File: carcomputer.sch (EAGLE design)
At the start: 76 parts, among them IC1 LM358N, K1 351, K2 RT184012, K3 RT184012, Q1 BS170, Q5 TIP136, T1 BC618, T2 BC618, T3 BC618, T4 BC618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

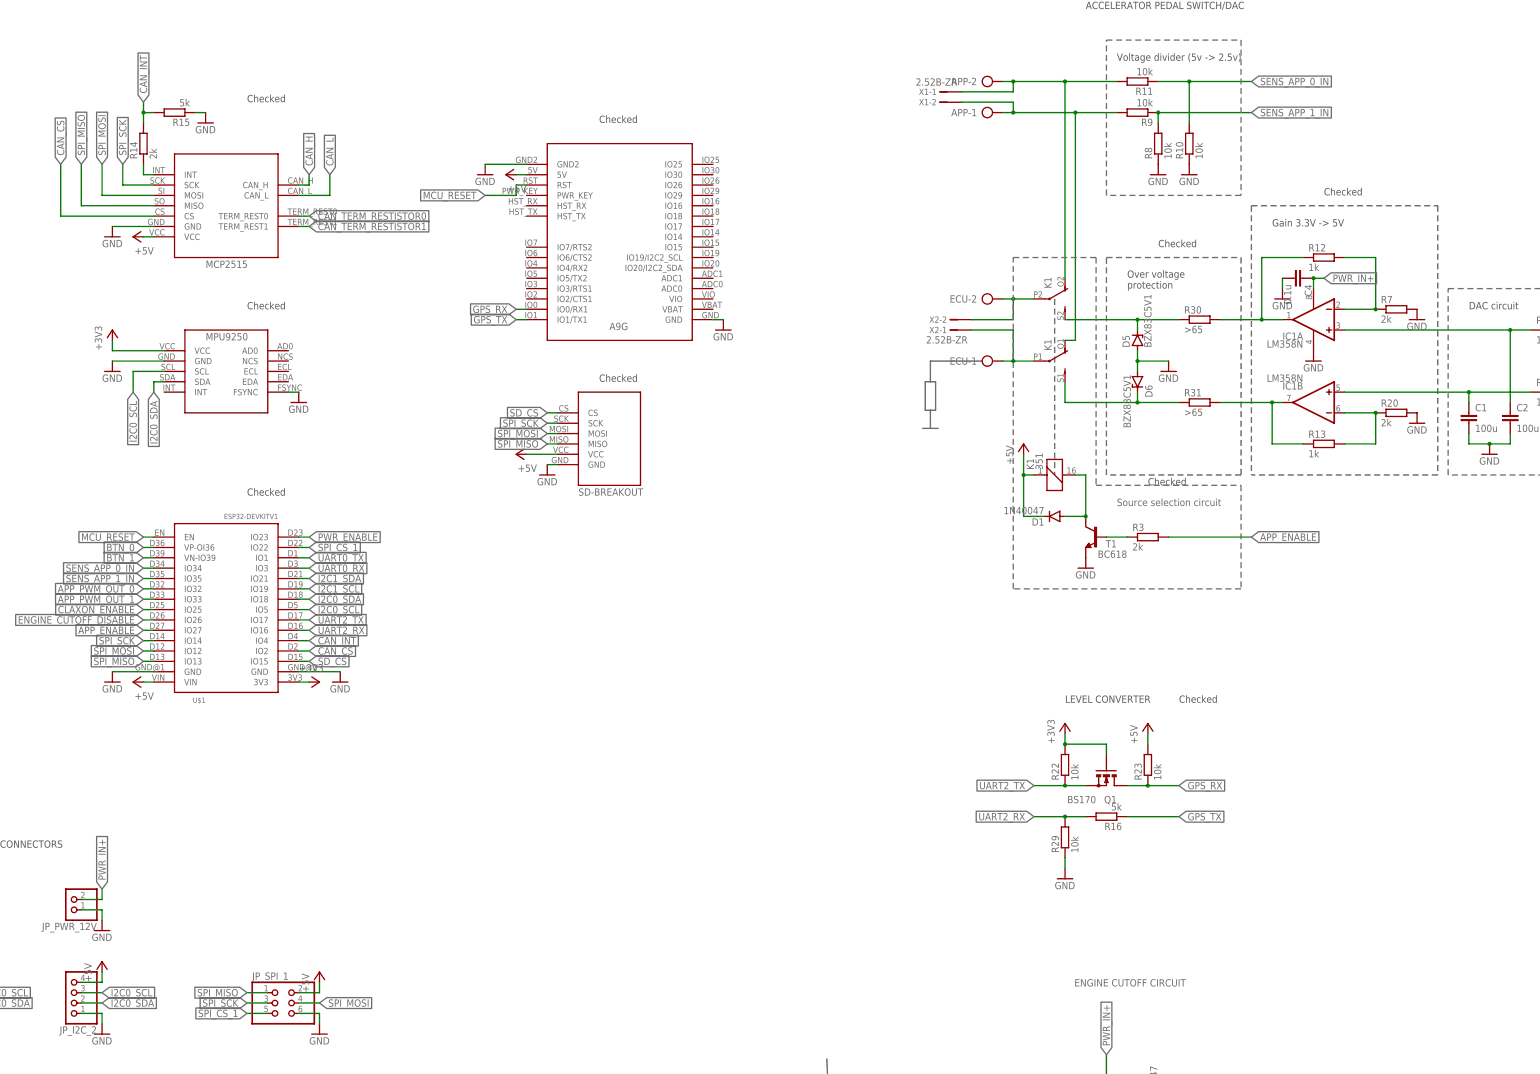
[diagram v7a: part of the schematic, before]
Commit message: Added volage divider for MISO. Also added more space to some tracks.
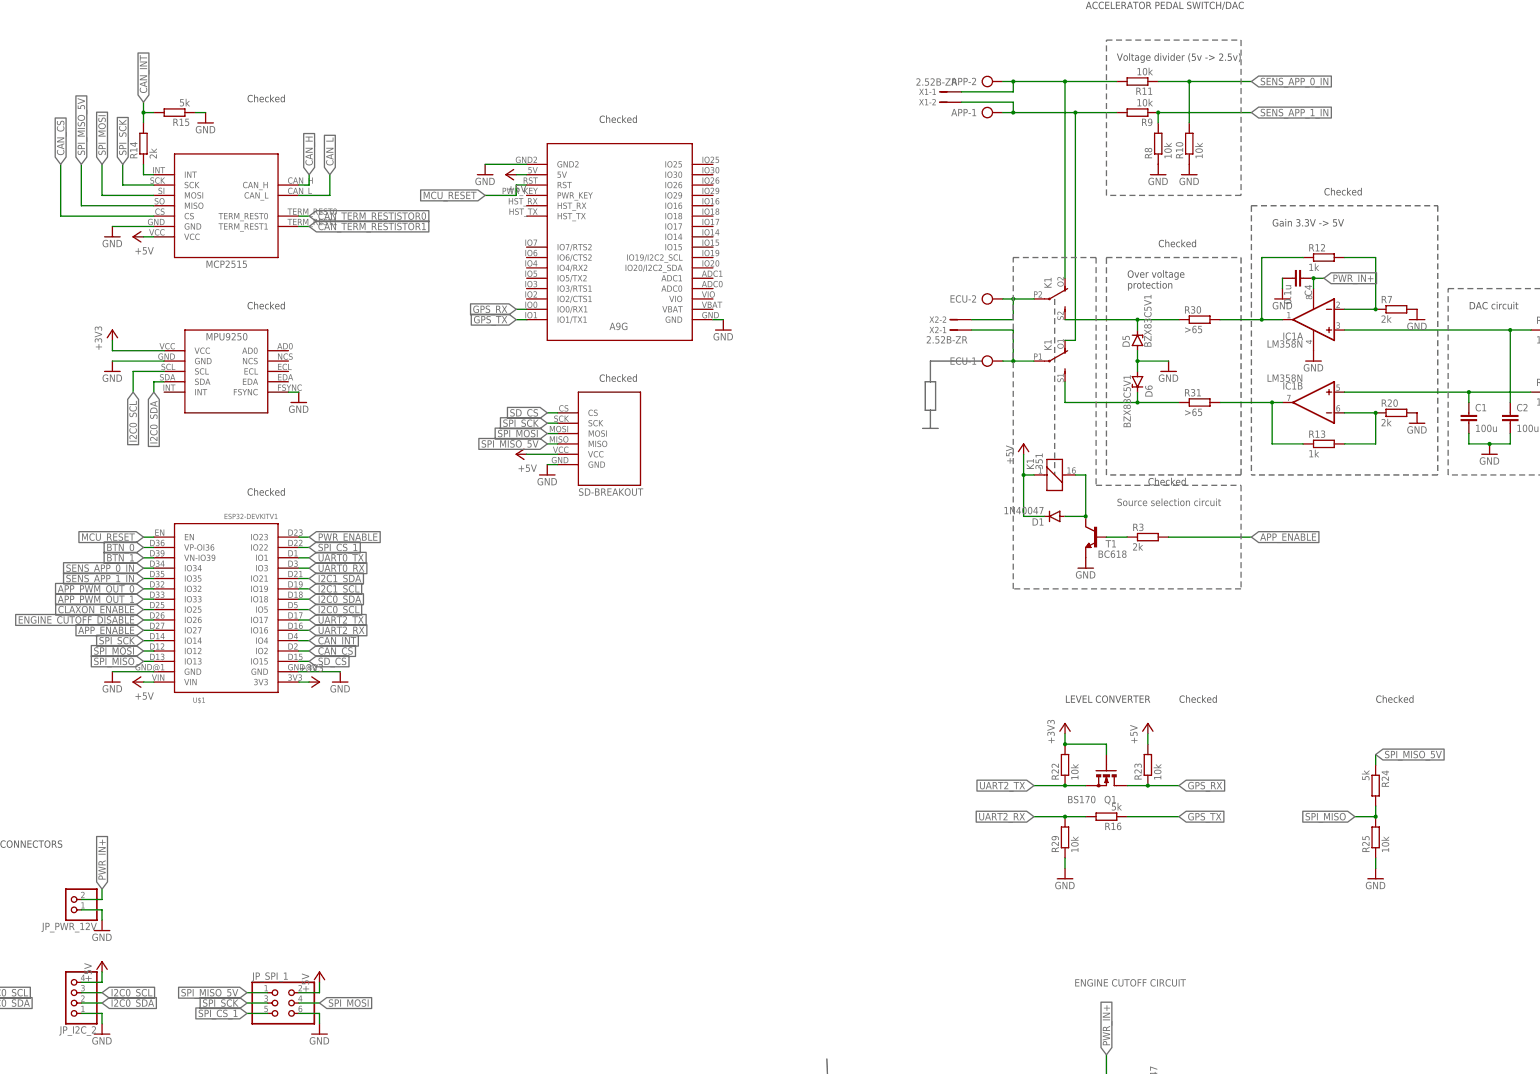
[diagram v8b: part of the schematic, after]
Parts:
- added R24: 5k, rcl:R-EU_0207/7
- added R25: 10k, rcl:R-EU_0207/7
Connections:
- new net SPI_MISO_5V: JP_SPI_1.1, R24.1, U$2.MISO, U$5.MISO
- net GND: now also R25.1
- net SPI_MISO: now also R24.2, R25.2; no longer JP_SPI_1.1, U$2.MISO, U$5.MISO
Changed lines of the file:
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@@
 <part name="X2" library="con-jst-custom" deviceset="?2B-ZR" device="2.5"/>
 <part name="CAN_TERM_RESISTOR" library="pinhead" library_urn="urn:adsk.eagle:library:325" deviceset="PINHD-1X2" device="" package3d_urn="urn:adsk.eagle:package:22435/2"/>
+<part name="GND22" library="supply1" library_urn="urn:adsk.eagle:library:371" deviceset="GND" device=""/>
+<part name="R24" library="rcl" library_urn="urn:adsk.eagle:library:334" deviceset="R-EU_" device="0207/7" package3d_urn="urn:adsk.eagle:package:23493/2" value="5k"/>
+<part name="R25" library="rcl" library_urn="urn:adsk.eagle:library:334" deviceset="R-EU_" device="0207/7" package3d_urn="urn:adsk.eagle:package:23493/2" value="10k"/>
 </parts>
 <sheets>
@@
 <wire x1="101.346" y1="-169.418" x2="101.346" y2="-168.656" width="0.1524" layer="97"/>
 <wire x1="101.346" y1="-169.418" x2="101.346" y2="-170.18" width="0.1524" layer="97"/>
+<text x="236.22" y="12.7" size="1.778" layer="97">Checked</text>
 </plain>
 <instances>
@@
 <attribute name="NAME" x="-176.53" y="-10.795" size="1.778" layer="95" rot="R180"/>
 <attribute name="VALUE" x="-176.53" y="0" size="1.778" layer="96" rot="R180"/>
+</instance>
+<instance part="GND22" gate="1" x="236.22" y="-30.48" smashed="yes">
+<attribute name="VALUE" x="233.68" y="-33.02" size="1.778" layer="96"/>
+</instance>
+<instance part="R24" gate="G$1" x="236.22" y="-7.62" smashed="yes" rot="R270">
+<attribute name="NAME" x="237.7186" y="-3.81" size="1.778" layer="95" rot="R270"/>
+<attribute name="VALUE" x="232.918" y="-3.81" size="1.778" layer="96" rot="R270"/>
+</instance>
+<instance part="R25" gate="G$1" x="236.22" y="-20.32" smashed="yes" rot="R90">
+<attribute name="NAME" x="234.7214" y="-24.13" size="1.778" layer="95" rot="R90"/>
+<attribute name="VALUE" x="239.522" y="-24.13" size="1.778" layer="96" rot="R90"/>
 </instance>
 </instances>
@@
 <wire x1="-162.56" y1="114.3" x2="-160.02" y2="114.3" width="0.1524" layer="91"/>
 </segment>
+<segment>
+<pinref part="R25" gate="G$1" pin="1"/>
+<pinref part="GND22" gate="1" pin="GND"/>
+<wire x1="236.22" y1="-25.4" x2="236.22" y2="-27.94" width="0.1524" layer="91"/>
+</segment>
 </net>
 <net name="+5V" class="0">
@@
 <net name="SPI_MISO" class="0">
 <segment>
-<pinref part="U$2" gate="G$1" pin="MISO"/>
-<wire x1="-63.5" y1="134.62" x2="-81.28" y2="134.62" width="0.1524" layer="91"/>
-<wire x1="-81.28" y1="134.62" x2="-81.28" y2="144.78" width="0.1524" layer="91"/>
-<label x="-81.28" y="144.78" size="1.778" layer="95" rot="R90" xref="yes"/>
-</segment>
-<segment>
-<pinref part="JP_SPI_1" gate="A" pin="1"/>
-<wire x1="-35.56" y1="-58.42" x2="-40.64" y2="-58.42" width="0.1524" layer="91"/>
-<label x="-40.64" y="-58.42" size="1.778" layer="95" rot="R180" xref="yes"/>
-</segment>
-<segment>
-<pinref part="U$5" gate="G$1" pin="MISO"/>
-<wire x1="35.56" y1="76.2" x2="33.02" y2="76.2" width="0.1524" layer="91"/>
-<label x="33.02" y="76.2" size="1.778" layer="95" rot="R180" xref="yes"/>
-</segment>
-<segment>
 <pinref part="U$1" gate="G$1" pin="IO13"/>
 <wire x1="-63.5" y1="22.86" x2="-66.04" y2="22.86" width="0.1524" layer="91"/>
 <label x="-66.04" y="22.86" size="1.778" layer="95" rot="R180" xref="yes"/>
+</segment>
+<segment>
+<pinref part="R24" gate="G$1" pin="2"/>
+<wire x1="231.14" y1="-15.24" x2="236.22" y2="-15.24" width="0.1524" layer="91"/>
+<pinref part="R25" gate="G$1" pin="2"/>
+<wire x1="236.22" y1="-15.24" x2="236.22" y2="-12.7" width="0.1524" layer="91"/>
+<junction x="236.22" y="-15.24"/>
+<label x="231.14" y="-15.24" size="1.778" layer="95" rot="R180" xref="yes"/>
 </segment>
 </net>
@@
 </segment>
 </net>
+<net name="SPI_MISO_5V" class="0">
+<segment>
+<pinref part="U$2" gate="G$1" pin="MISO"/>
+<wire x1="-63.5" y1="134.62" x2="-81.28" y2="134.62" width="0.1524" layer="91"/>
+<wire x1="-81.28" y1="134.62" x2="-81.28" y2="144.78" width="0.1524" layer="91"/>
+<label x="-81.28" y="144.78" size="1.778" layer="95" rot="R90" xref="yes"/>
+</segment>
+<segment>
+<pinref part="U$5" gate="G$1" pin="MISO"/>
+<wire x1="35.56" y1="76.2" x2="33.02" y2="76.2" width="0.1524" layer="91"/>
+<label x="33.02" y="76.2" size="1.778" layer="95" rot="R180" xref="yes"/>
+</segment>
+<segment>
+<wire x1="236.22" y1="-2.54" x2="236.22" y2="0" width="0.1524" layer="91"/>
+<pinref part="R24" gate="G$1" pin="1"/>
+<label x="236.22" y="0" size="1.778" layer="95" xref="yes"/>
+</segment>
+<segment>
+<pinref part="JP_SPI_1" gate="A" pin="1"/>
+<wire x1="-35.56" y1="-58.42" x2="-40.64" y2="-58.42" width="0.1524" layer="91"/>
+<label x="-40.64" y="-58.42" size="1.778" layer="95" rot="R180" xref="yes"/>
+</segment>
+</net>
